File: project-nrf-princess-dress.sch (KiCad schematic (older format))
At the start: 1 part

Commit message: First schematic draft
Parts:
- added C1, C2, C4, C5, C7, C8: 0.1uF, Capacitor_SMD:C_0603_1608Metric, symbol Device:C
- added C3, C6, C9: 22uF, Capacitor_SMD:C_1210_3225Metric, symbol Device:C
- added J1: Conn_01x02_Female, TZ022101B000G:TZ022101B000G, symbol Connector:Conn_01x02_Female
- added J2, J4, J7: Conn_01x04_Female, TZ042101B000G:TZ042101B000G, symbol Connector:Conn_01x04_Female
- added J3, J5: Conn_01x12_Female, Connector_PinSocket_2.54mm:PinSocket_1x12_P2.54mm_Vertical_SMD_Pin1Right, symbol Connector:Conn_01x12_Female
- added J6: Conn_01x01_Female, Connector_Wire:SolderWirePad_1x01_SMD_5x10mm, symbol Connector:Conn_01x01_Female
- added J8: SM04B-SRSS-TB(LF)(SN), SM04B-SRSS-TB(LF)(SN):JST_SM04B-SRSS-TB(LF)(SN), symbol SM04B-SRSS-TB_LF__SN_:SM04B-SRSS-TB(LF)(SN)
- added Q1: Q_PMOS_GSD, Package_TO_SOT_SMD:SOT-23, symbol Device:Q_PMOS_GSD
- added R1: 0ZCJ0050AF2E, 0ZCJ0050AF2E:RESC3216X125N, symbol 0ZCJ0050AF2E:0ZCJ0050AF2E
- added R2: 10k, Resistor_SMD:R_0603_1608Metric, symbol Device:R
- added S1: CL-SB-22A-02T, CL-SB-22A-02T:SW_CL-SB-22A-02T, symbol CL-SB-22A-02T:CL-SB-22A-02T
- added U1, U2: TXU0204BQAR, TXU0204BQAR:TXU0204BQAR, symbol TXU0204BQAR:TXU0204BQAR
- gave numbers to parts that had none: 1
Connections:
- net VDD: now reaches U3.1 (VCCA)
- net VDD: now also U3.8 (OE), C1.1, C4.1, C7.1, J5.12 (Pin_12), U1.1 (VCCA), U1.8 (OE), U2.1 (VCCA), U2.8 (OE)
- net at U3.12 (B2Y): now also J7.3 (Pin_3)
- net at U3.13 (B1Y): now also J7.2 (Pin_2)
- net +BATT: now reaches U3.14 (VCCB)
- net +BATT: now also C2.1, C3.1, C5.1, C6.1, C8.1, C9.1, J2.1 (Pin_1), J4.1 (Pin_1), J5.10 (Pin_10), J7.1 (Pin_1), J8.2, Q1.3 (D), U1.14 (VCCB), U2.14 (VCCB)
- net P1.15: now reaches U3.2 (A1)
- net P1.15: now also J5.5 (Pin_5)
- net P0.02: now reaches U3.3 (A2)
- net P0.02: now also J5.6 (Pin_6)
- net GND: now reaches U3.7 (GND)
- net GND: now also C1.2, C2.2, C3.2, C4.2, C5.2, C6.2, C7.2, C8.2, C9.2, J1.2 (Pin_2), J2.4 (Pin_4), J3.12 (Pin_12), J4.4 (Pin_4), J7.4 (Pin_4), J8.1, J8.S1 (SHIELD), J8.S2 (SHIELD), S1.3, U1.7 (GND), U2.7 (GND)
- new net: J1.1 (Pin_1), R1.1
- new net: Q1.2 (S), R1.2, R2.1
- new net: Q1.1 (G), R2.2, S1.2
- new net: J4.3 (Pin_3), U2.12 (B2Y)
- new net: J4.2 (Pin_2), U2.13 (B1Y)
- new net: J2.3 (Pin_3), U1.12 (B2Y)
- new net: J2.2 (Pin_2), U1.13 (B1Y)
- new net P0.03: J5.3 (Pin_3), U2.2 (A1)
- new net P0.04: J5.9 (Pin_9)
- new net P0.05: J5.8 (Pin_8)
- new net P0.09: J3.1 (Pin_1), J8.3
- new net P0.10: J3.2 (Pin_2), J8.4
- new net P0.13: J3.8 (Pin_8)
- new net P0.15: J3.9 (Pin_9)
- new net P0.17: J3.10 (Pin_10)
- new net P0.19: J3.7 (Pin_7)
- new net P0.21: J3.11 (Pin_11)
- new net P0.22: J3.4 (Pin_4), J6.1 (Pin_1)
- new net P0.23: J3.6 (Pin_6)
- new net P0.29: J5.7 (Pin_7)
- new net P1.03: J5.4 (Pin_4), U2.3 (A2)
- new net P1.10: J5.1 (Pin_1), U1.2 (A1)
- new net P1.14: J5.2 (Pin_2), U1.3 (A2)
- new net RX: J3.3 (Pin_3)
- new net TX: J3.5 (Pin_5)
- no-connect marks 0 -> 28
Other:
- note added: "CAUTION: BOARD MOUNTED BACK FACING UP!"
- note added: "PIN2"
- moved on the sheet: U3

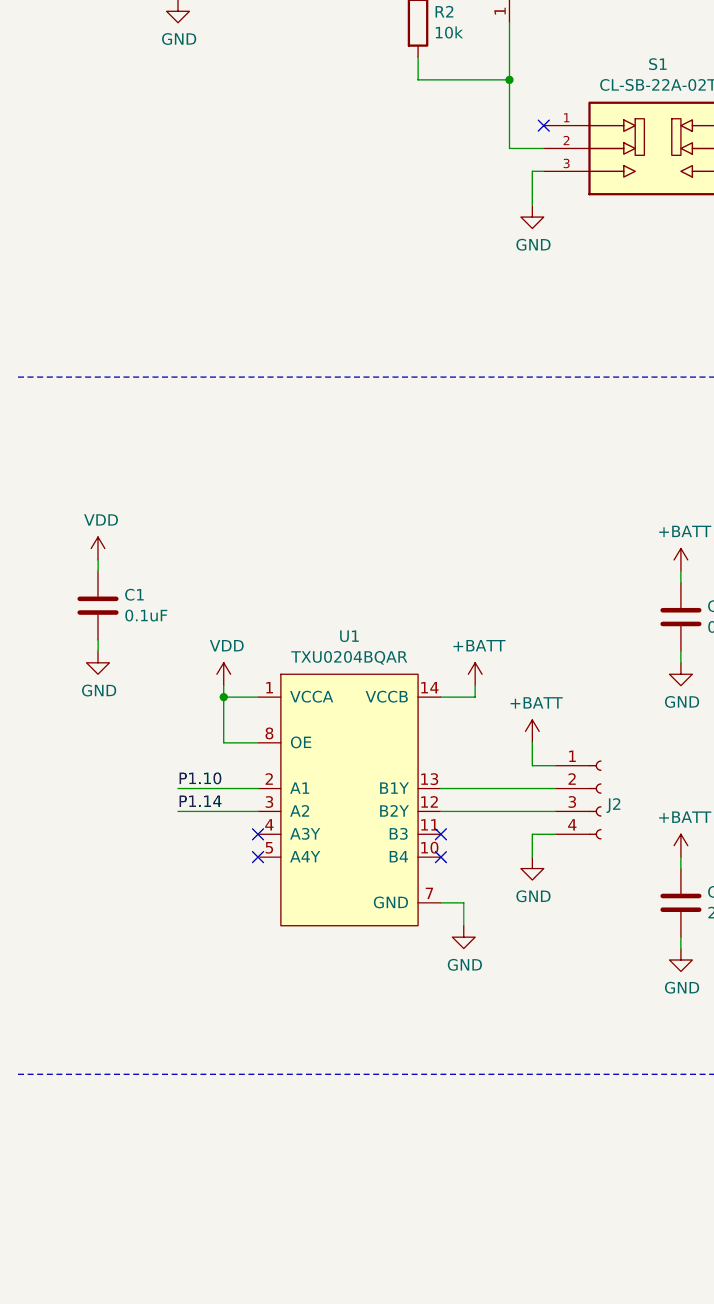
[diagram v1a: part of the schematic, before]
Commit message: Add mounting holes
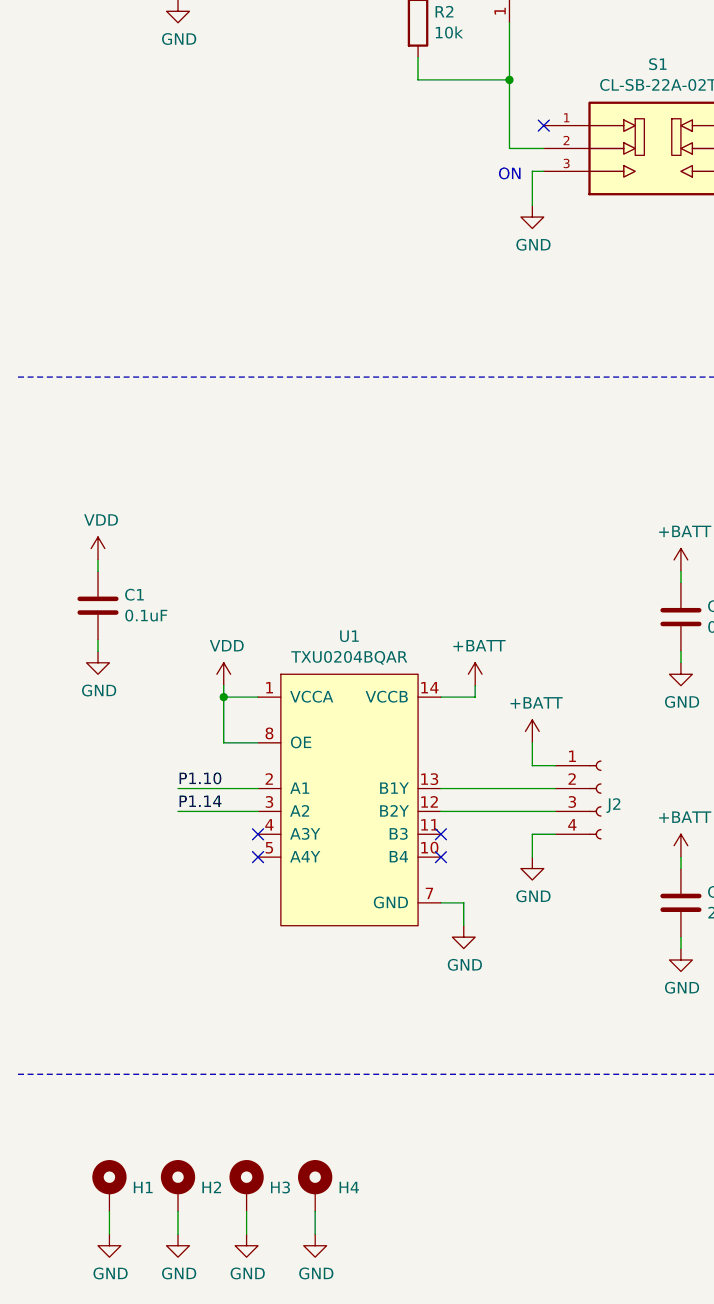
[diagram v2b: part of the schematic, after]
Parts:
- added H1, H2, H3, H4: MountingHole_Pad, MountingHole:MountingHole_2.7mm_M2.5_ISO7380_Pad, symbol Mechanical:MountingHole_Pad
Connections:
- net GND: now also H1.1, H2.1, H3.1, H4.1
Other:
- note added: "ON"
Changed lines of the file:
@@
 Wire Wire Line
 	9650 5250 9650 5350
+$Comp
+L Mechanical:MountingHole_Pad H1
+U 1 1 638FF080
+P 900 6400
+F 0 "H1" H 1000 6403 50  0000 L CNN
+F 1 "MountingHole_Pad" H 1000 6358 50  0001 L CNN
+F 2 "MountingHole:MountingHole_2.7mm_M2.5_ISO7380_Pad" H 900 6400 50  0001 C CNN
+F 3 "~" H 900 6400 50  0001 C CNN
+	1    900  6400
+	1    0    0    -1
+$EndComp
+$Comp
+L power:GND #PWR01
+U 1 1 63900116
+P 900 6600
+F 0 "#PWR01" H 900 6350 50  0001 C CNN
+F 1 "GND" H 905 6427 50  0000 C CNN
+F 2 "" H 900 6600 50  0001 C CNN
+F 3 "" H 900 6600 50  0001 C CNN
+	1    900  6600
+	1    0    0    -1
+$EndComp
+Wire Wire Line
+	900  6500 900  6600
+$Comp
+L Mechanical:MountingHole_Pad H2
+U 1 1 6390AB68
+P 1200 6400
+F 0 "H2" H 1300 6403 50  0000 L CNN
+F 1 "MountingHole_Pad" H 1300 6358 50  0001 L CNN
+F 2 "MountingHole:MountingHole_2.7mm_M2.5_ISO7380_Pad" H 1200 6400 50  0001 C CNN
+F 3 "~" H 1200 6400 50  0001 C CNN
+	1    1200 6400
+	1    0    0    -1
+$EndComp
+$Comp
+L power:GND #PWR02
+U 1 1 6390AB6E
+P 1200 6600
+F 0 "#PWR02" H 1200 6350 50  0001 C CNN
+F 1 "GND" H 1205 6427 50  0000 C CNN
+F 2 "" H 1200 6600 50  0001 C CNN
+F 3 "" H 1200 6600 50  0001 C CNN
+	1    1200 6600
+	1    0    0    -1
+$EndComp
+Wire Wire Line
+	1200 6500 1200 6600
+$Comp
+L Mechanical:MountingHole_Pad H3
+U 1 1 6390EF9F
+P 1500 6400
+F 0 "H3" H 1600 6403 50  0000 L CNN
+F 1 "MountingHole_Pad" H 1600 6358 50  0001 L CNN
+F 2 "MountingHole:MountingHole_2.7mm_M2.5_ISO7380_Pad" H 1500 6400 50  0001 C CNN
+F 3 "~" H 1500 6400 50  0001 C CNN
+	1    1500 6400
+	1    0    0    -1
+$EndComp
+$Comp
+L power:GND #PWR03
+U 1 1 6390EFA5
+P 1500 6600
+F 0 "#PWR03" H 1500 6350 50  0001 C CNN
+F 1 "GND" H 1505 6427 50  0000 C CNN
+F 2 "" H 1500 6600 50  0001 C CNN
+F 3 "" H 1500 6600 50  0001 C CNN
+	1    1500 6600
+	1    0    0    -1
+$EndComp
+Wire Wire Line
+	1500 6500 1500 6600
+$Comp
+L Mechanical:MountingHole_Pad H4
+U 1 1 63913532
+P 1800 6400
+F 0 "H4" H 1900 6403 50  0000 L CNN
+F 1 "MountingHole_Pad" H 1900 6358 50  0001 L CNN
+F 2 "MountingHole:MountingHole_2.7mm_M2.5_ISO7380_Pad" H 1800 6400 50  0001 C CNN
+F 3 "~" H 1800 6400 50  0001 C CNN
+	1    1800 6400
+	1    0    0    -1
+$EndComp
+$Comp
+L power:GND #PWR04
+U 1 1 63913538
+P 1800 6600
+F 0 "#PWR04" H 1800 6350 50  0001 C CNN
+F 1 "GND" H 1805 6427 50  0000 C CNN
+F 2 "" H 1800 6600 50  0001 C CNN
+F 3 "" H 1800 6600 50  0001 C CNN
+	1    1800 6600
+	1    0    0    -1
+$EndComp
+Wire Wire Line
+	1800 6500 1800 6600
+Text Notes 2600 2000 0    50   ~ 0
+ON
 $EndSCHEMATC

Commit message: First placement
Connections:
- net +BATT: no longer J8.2
- net VDD: now also J8.2
- net at U3.12 (B2Y): now also J7.2 (Pin_2); no longer J7.3 (Pin_3)
- net at U3.13 (B1Y): now also J7.3 (Pin_3); no longer J7.2 (Pin_2)
- net at U2.12 (B2Y): now also J4.2 (Pin_2); no longer J4.3 (Pin_3)
- net at U2.13 (B1Y): now also J4.3 (Pin_3); no longer J4.2 (Pin_2)
- net at U1.12 (B2Y): now also J2.2 (Pin_2); no longer J2.3 (Pin_3)
- net at U1.13 (B1Y): now also J2.3 (Pin_3); no longer J2.2 (Pin_2)
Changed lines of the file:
@@
 Text Label 1000 1100 0    50   ~ 0
 GND
-Text Label 2950 1000 0    50   ~ 0
-VCC
 Wire Wire Line
 	1250 1100 1200 1100
@@
 Text Label 9750 1600 0    50   ~ 0
 GND
-Text Label 9750 1700 0    50   ~ 0
-VCC
 Text Label 9750 1800 0    50   ~ 0
 SDA
@@
 Wire Wire Line
 	9750 1600 10050 1600
-Wire Wire Line
-	9750 1700 10050 1700
 Wire Wire Line
 	9750 1800 10050 1800
@@
 L Connector:Conn_01x04_Female J4
 U 1 1 637A4856
-P 6800 4700
-F 0 "J4" H 6828 4630 50  0000 L CNN
-F 1 "Conn_01x04_Female" H 6828 4585 50  0001 L CNN
-F 2 "TZ042101B000G:TZ042101B000G" H 6800 4700 50  0001 C CNN
-F 3 "~" H 6800 4700 50  0001 C CNN
-	1    6800 4700
-	1    0    0    -1
+P 6800 4800
+F 0 "J4" H 6692 4467 50  0000 C CNN
+F 1 "Conn_01x04_Female" H 6828 4685 50  0001 L CNN
+F 2 "TZ042101B000G:TZ042101B000G" H 6800 4800 50  0001 C CNN
+F 3 "~" H 6800 4800 50  0001 C CNN
+	1    6800 4800
+	1    0    0    1
 $EndComp
 $Comp
@@
 NoConn ~ 6100 4900
 NoConn ~ 6100 5000
-$Comp
-L power:+BATT #PWR0116
-U 1 1 637A48B3
-P 6500 4500
-F 0 "#PWR0116" H 6500 4350 50  0001 C CNN
-F 1 "+BATT" H 6515 4673 50  0000 C CNN
-F 2 "" H 6500 4500 50  0001 C CNN
-F 3 "" H 6500 4500 50  0001 C CNN
-	1    6500 4500
-	1    0    0    -1
-$EndComp
-Wire Wire Line
-	6500 4500 6500 4600
-Wire Wire Line
-	6500 4600 6600 4600
-$Comp
-L power:GND #PWR0117
-U 1 1 637A48BB
-P 6500 5000
-F 0 "#PWR0117" H 6500 4750 50  0001 C CNN
-F 1 "GND" H 6505 4827 50  0000 C CNN
-F 2 "" H 6500 5000 50  0001 C CNN
-F 3 "" H 6500 5000 50  0001 C CNN
-	1    6500 5000
-	1    0    0    -1
-$EndComp
-Wire Wire Line
-	6500 5000 6500 4900
-Wire Wire Line
-	6500 4900 6600 4900
 Wire Wire Line
 	6100 4700 6600 4700
@@
 $EndComp
 $Comp
-L Connector:Conn_01x04_Female J2
-U 1 1 637A9D9B
-P 3050 4650
-F 0 "J2" H 3078 4580 50  0000 L CNN
-F 1 "Conn_01x04_Female" H 3078 4535 50  0001 L CNN
-F 2 "TZ042101B000G:TZ042101B000G" H 3050 4650 50  0001 C CNN
-F 3 "~" H 3050 4650 50  0001 C CNN
-	1    3050 4650
-	1    0    0    -1
-$EndComp
-$Comp
 L Device:C C3
 U 1 1 637A9DA1
@@
 Wire Wire Line
 	1550 4750 1200 4750
-$Comp
-L power:+BATT #PWR0126
-U 1 1 637A9DF8
-P 2750 4450
-F 0 "#PWR0126" H 2750 4300 50  0001 C CNN
-F 1 "+BATT" H 2765 4623 50  0000 C CNN
-F 2 "" H 2750 4450 50  0001 C CNN
-F 3 "" H 2750 4450 50  0001 C CNN
-	1    2750 4450
-	1    0    0    -1
-$EndComp
-Wire Wire Line
-	2750 4450 2750 4550
-Wire Wire Line
-	2750 4550 2850 4550
-$Comp
-L power:GND #PWR0127
-U 1 1 637A9E00
-P 2750 4950
-F 0 "#PWR0127" H 2750 4700 50  0001 C CNN
-F 1 "GND" H 2755 4777 50  0000 C CNN
-F 2 "" H 2750 4950 50  0001 C CNN
-F 3 "" H 2750 4950 50  0001 C CNN
-	1    2750 4950
-	1    0    0    -1
-$EndComp
-Wire Wire Line
-	2750 4950 2750 4850
-Wire Wire Line
-	2750 4850 2850 4850
 Wire Wire Line
 	2350 4650 2850 4650
@@
 Wire Wire Line
 	9950 4950 10050 4950
-Wire Wire Line
-	9950 5050 9950 4950
 $Comp
 L power:GND #PWR0128
 U 1 1 63788944
-P 9950 5050
-F 0 "#PWR0128" H 9950 4800 50  0001 C CNN
-F 1 "GND" H 9955 4877 50  0000 C CNN
-F 2 "" H 9950 5050 50  0001 C CNN
-F 3 "" H 9950 5050 50  0001 C CNN
-	1    9950 5050
+P 9800 4450
+F 0 "#PWR0128" H 9800 4200 50  0001 C CNN
+F 1 "GND" H 9805 4277 50  0000 C CNN
+F 2 "" H 9800 4450 50  0001 C CNN
+F 3 "" H 9800 4450 50  0001 C CNN
+	1    9800 4450
 	1    0    0    -1
 $EndComp
 Wire Wire Line
 	9950 4650 10050 4650
-Wire Wire Line
-	9950 4550 9950 4650
-$Comp
-L power:+BATT #PWR0129
-U 1 1 63786B05
-P 9950 4550
-F 0 "#PWR0129" H 9950 4400 50  0001 C CNN
-F 1 "+BATT" H 9965 4723 50  0000 C CNN
-F 2 "" H 9950 4550 50  0001 C CNN
-F 3 "" H 9950 4550 50  0001 C CNN
-	1    9950 4550
-	1    0    0    -1
-$EndComp
 NoConn ~ 9550 5050
 NoConn ~ 9550 4950
@@
 L Connector:Conn_01x04_Female J7
 U 1 1 636497F0
-P 10250 4750
-F 0 "J7" H 10278 4680 50  0000 L CNN
-F 1 "Conn_01x04_Female" H 10278 4635 50  0001 L CNN
-F 2 "TZ042101B000G:TZ042101B000G" H 10250 4750 50  0001 C CNN
-F 3 "~" H 10250 4750 50  0001 C CNN
-	1    10250 4750
-	1    0    0    -1
+P 10250 4850
+F 0 "J7" H 10142 4517 50  0000 C CNN
+F 1 "Conn_01x04_Female" H 10278 4735 50  0001 L CNN
+F 2 "TZ042101B000G:TZ042101B000G" H 10250 4850 50  0001 C CNN
+F 3 "~" H 10250 4850 50  0001 C CNN
+	1    10250 4850
+	1    0    0    1
 $EndComp
 $Comp
@@
 Text Notes 2600 2000 0    50   ~ 0
 ON
+$Comp
+L Connector:Conn_01x04_Female J2
+U 1 1 637A9D9B
+P 3050 4750
+F 0 "J2" H 2942 4417 50  0000 C CNN
+F 1 "Conn_01x04_Female" H 3078 4635 50  0001 L CNN
+F 2 "TZ042101B000G:TZ042101B000G" H 3050 4750 50  0001 C CNN
+F 3 "~" H 3050 4750 50  0001 C CNN
+	1    3050 4750
+	1    0    0    1
+$EndComp
+Wire Wire Line
+	9800 4450 9800 4400
+Wire Wire Line
+	9800 4400 9950 4400
+Wire Wire Line
+	9950 4400 9950 4650
+$Comp
+L power:GND #PWR0116
+U 1 1 639B2124
+P 2600 4350
+F 0 "#PWR0116" H 2600 4100 50  0001 C CNN
+F 1 "GND" H 2605 4177 50  0000 C CNN
+F 2 "" H 2600 4350 50  0001 C CNN
+F 3 "" H 2600 4350 50  0001 C CNN
+	1    2600 4350
+	1    0    0    -1
+$EndComp
+Wire Wire Line
+	2750 4550 2850 4550
+Wire Wire Line
+	2600 4350 2600 4300
+Wire Wire Line
+	2600 4300 2750 4300
+Wire Wire Line
+	2750 4300 2750 4550
+$Comp
+L power:GND #PWR0117
+U 1 1 639B6CE3
+P 6350 4400
+F 0 "#PWR0117" H 6350 4150 50  0001 C CNN
+F 1 "GND" H 6355 4227 50  0000 C CNN
+F 2 "" H 6350 4400 50  0001 C CNN
+F 3 "" H 6350 4400 50  0001 C CNN
+	1    6350 4400
+	1    0    0    -1
+$EndComp
+Wire Wire Line
+	6500 4600 6600 4600
+Wire Wire Line
+	6350 4400 6350 4350
+Wire Wire Line
+	6350 4350 6500 4350
+Wire Wire Line
+	6500 4350 6500 4600
+Wire Wire Line
+	9950 4950 9950 5150
+Wire Wire Line
+	9800 5150 9950 5150
+Wire Wire Line
+	9800 5100 9800 5150
+$Comp
+L power:+BATT #PWR0129
+U 1 1 63786B05
+P 9800 5100
+F 0 "#PWR0129" H 9800 4950 50  0001 C CNN
+F 1 "+BATT" H 9815 5273 50  0000 C CNN
+F 2 "" H 9800 5100 50  0001 C CNN
+F 3 "" H 9800 5100 50  0001 C CNN
+	1    9800 5100
+	1    0    0    -1
+$EndComp
+Wire Wire Line
+	6500 4900 6600 4900
+Wire Wire Line
+	6500 4900 6500 5100
+Wire Wire Line
+	6350 5100 6500 5100
+Wire Wire Line
+	6350 5050 6350 5100
+$Comp
+L power:+BATT #PWR0126
+U 1 1 639D2140
+P 6350 5050
+F 0 "#PWR0126" H 6350 4900 50  0001 C CNN
+F 1 "+BATT" H 6365 5223 50  0000 C CNN
+F 2 "" H 6350 5050 50  0001 C CNN
+F 3 "" H 6350 5050 50  0001 C CNN
+	1    6350 5050
+	1    0    0    -1
+$EndComp
+Wire Wire Line
+	2750 4850 2850 4850
+Wire Wire Line
+	2750 4850 2750 5050
+Wire Wire Line
+	2600 5050 2750 5050
+Wire Wire Line
+	2600 5000 2600 5050
+$Comp
+L power:+BATT #PWR0127
+U 1 1 639D82E4
+P 2600 5000
+F 0 "#PWR0127" H 2600 4850 50  0001 C CNN
+F 1 "+BATT" H 2615 5173 50  0000 C CNN
+F 2 "" H 2600 5000 50  0001 C CNN
+F 3 "" H 2600 5000 50  0001 C CNN
+	1    2600 5000
+	1    0    0    -1
+$EndComp
+$Comp
+L power:VDD #PWR?
+U 1 1 63A0DCF7
+P 9600 1600
+F 0 "#PWR?" H 9600 1450 50  0001 C CNN
+F 1 "VDD" H 9615 1773 50  0000 C CNN
+F 2 "" H 9600 1600 50  0001 C CNN
+F 3 "" H 9600 1600 50  0001 C CNN
+	1    9600 1600
+	1    0    0    -1
+$EndComp
+Wire Wire Line
+	9600 1700 9600 1600
+Wire Wire Line
+	9600 1700 10050 1700
 $EndSCHEMATC

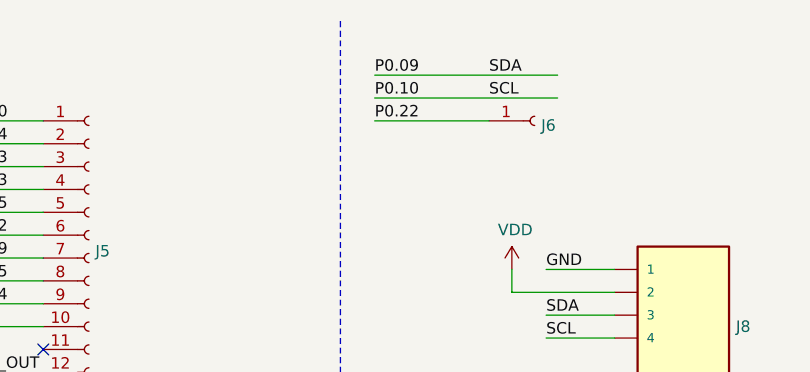
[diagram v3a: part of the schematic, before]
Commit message: Change i2c pins order
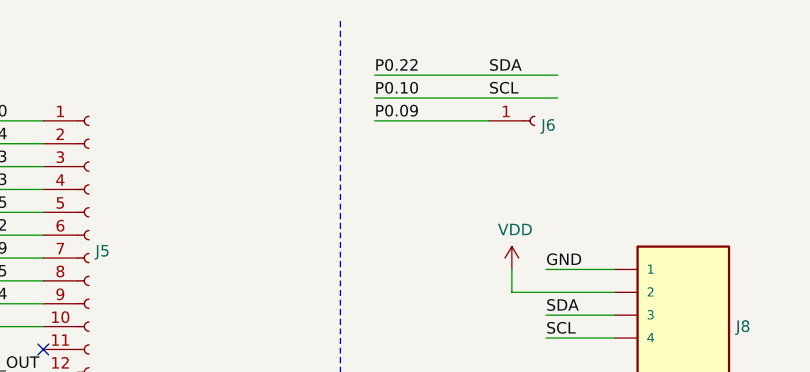
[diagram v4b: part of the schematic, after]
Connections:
- net P0.09: now also J6.1 (Pin_1); no longer J8.3
- net P0.22: now also J8.3; no longer J6.1 (Pin_1)
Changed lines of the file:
@@
 Text Label 9500 850  0    50   ~ 0
 SCL
-Text Label 9000 750  0    50   ~ 0
+Text Label 9000 950  0    50   ~ 0
 P0.09
 Text Label 9000 850  0    50   ~ 0
 P0.10
-Text Label 9000 950  0    50   ~ 0
+Text Label 9000 750  0    50   ~ 0
 P0.22
 $Comp
@@
 $EndComp
 $Comp
-L power:VDD #PWR?
+L power:VDD #PWR0141
 U 1 1 63A0DCF7
 P 9600 1600
-F 0 "#PWR?" H 9600 1450 50  0001 C CNN
+F 0 "#PWR0141" H 9600 1450 50  0001 C CNN
 F 1 "VDD" H 9615 1773 50  0000 C CNN
 F 2 "" H 9600 1600 50  0001 C CNN

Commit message: Routing
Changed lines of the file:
@@
 	9600 1700 9600 1600
 Wire Wire Line
-	9600 1700 10050 1700
+	10050 1700 9600 1700
 $EndSCHEMATC

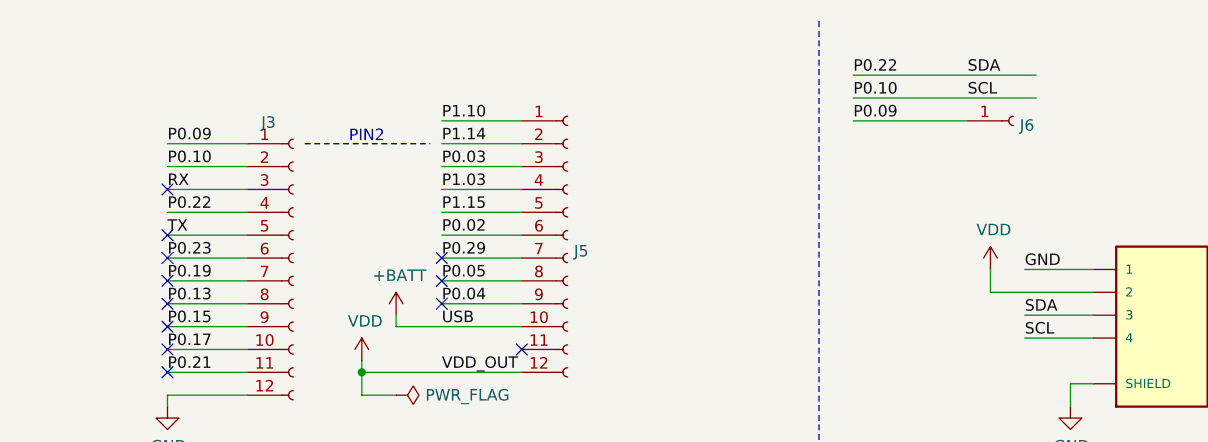
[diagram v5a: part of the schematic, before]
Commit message: Add a pad for the ism330dhcx int2
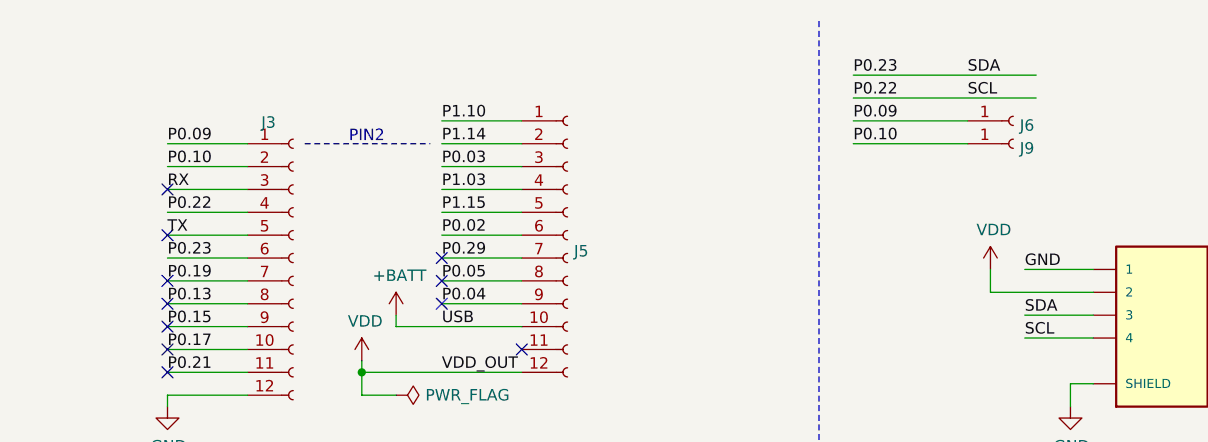
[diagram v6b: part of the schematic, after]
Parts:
- added J9: Conn_01x01_Female, Connector_Wire:SolderWirePad_1x01_SMD_5x10mm, symbol Connector:Conn_01x01_Female
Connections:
- net P0.10: now also J9.1 (Pin_1); no longer J8.4
- net P0.22: now also J8.4; no longer J8.3
- net P0.23: now also J8.3
- no-connect marks 28 -> 27
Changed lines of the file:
@@
 P0.09
 Text Label 9000 850  0    50   ~ 0
-P0.10
+P0.22
 Text Label 9000 750  0    50   ~ 0
-P0.22
+P0.23
 $Comp
 L Connector:Conn_01x01_Female J6
@@
 NoConn ~ 6000 1250
 NoConn ~ 6000 1450
-NoConn ~ 6000 1550
 NoConn ~ 6000 1650
 NoConn ~ 6000 1750
@@
 Wire Wire Line
 	10050 1700 9600 1700
+Text Label 9000 1050 0    50   ~ 0
+P0.10
+$Comp
+L Connector:Conn_01x01_Female J9
+U 1 1 6393BC48
+P 9700 1050
+F 0 "J9" H 9728 1030 50  0000 L CNN
+F 1 "Conn_01x01_Female" H 9728 985 50  0001 L CNN
+F 2 "Connector_Wire:SolderWirePad_1x01_SMD_5x10mm" H 9700 1050 50  0001 C CNN
+F 3 "~" H 9700 1050 50  0001 C CNN
+	1    9700 1050
+	1    0    0    -1
+$EndComp
+Wire Wire Line
+	9000 1050 9500 1050
 $EndSCHEMATC
